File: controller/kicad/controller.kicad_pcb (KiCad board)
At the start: 2 copper layers, 90 x 80 mm, 27 parts, among them J1 pcie_98, U1 WeAct_STM32H750_Module, U10 ESD5344D, U11 ESD5344D, U12 ESD5344D, U13 ESD5344D, U14 ESD5344D, U15 ESD5344D, U16 ESD5344D, U17 ESD5344D, U18 ESD5344D, U19 ESD5344D, U2 ESD5344D, U20 ESD5344D, U21 ESD5344D, U3 ESD5344D, U4 ESD5344D, U5 ESD5344D, U6 ESD5344D, U7 ESD5344D, U8 ESD5344D, U9 ESD5344D

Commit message: Added Controller doc and added an optional jumper to short the Schottky diode.
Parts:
- added R1: 0R, Resistor_SMD:R_0805_2012Metric, F.Cu at (56.3, 38.7)
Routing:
- net /+5VBUS: track 36.5 -> 39.0 mm
- net /+5V: track 139.9 -> 142.4 mm
- net /PB13: track 88.2 -> 87.3 mm
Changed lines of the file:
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@@
     (property "ki_keywords" "diode Schottky")
     (attr smd)
-    (fp_text reference "D1" (at 0 -2.1942 -180) (layer "F.SilkS")
+    (fp_text reference "D1" (at -0.0762 2.073 -180) (layer "F.SilkS")
         (effects (font (size 1 1) (thickness 0.15)))
     )
@@
     (property "ki_keywords" "cap capacitor")
     (attr smd)
-    (fp_text reference "C2" (at 0 -3.7) (layer "F.SilkS")
+    (fp_text reference "C2" (at -0.086 3.8354) (layer "F.SilkS")
         (effects (font (size 1 1) (thickness 0.15)))
     )
@@
       (scale (xyz 1 1 1))
       (rotate (xyz 0 0 90))
+    )
+  )
+  (footprint "Resistor_SMD:R_0805_2012Metric" (layer "F.Cu")
+    (at 56.261 38.6842 90)
+    (descr "Resistor SMD 0805 (2012 Metric), square (rectangular) end terminal, IPC_7351 nominal, (Body size source: IPC-SM-782 page 72, https://www.pcb-3d.com/wordpress/wp-content/uploads/ipc-sm-782a_amendment_1_and_2.pdf), generated with kicad-footprint-generator")
+    (tags "resistor")
+    (property "LCSC" "C17477")
+    (property "Sheetfile" "controller.kicad_sch")
+    (property "Sheetname" "")
+    (property "dnp" "")
+    (property "exclude_from_bom" "")
+    (property "ki_description" "Resistor, US symbol")
+    (property "ki_keywords" "R res resistor")
+    (attr smd exclude_from_bom)
+    (fp_text reference "R1" (at -0.1524 1.8796 180) (layer "F.SilkS")
+        (effects (font (size 1 1) (thickness 0.15)))
+    )
+    (fp_text value "0R" (at 0 1.65 90) (layer "F.Fab")
+        (effects (font (size 1 1) (thickness 0.15)))
+    )
+    (fp_text user "${REFERENCE}" (at 0 0 90) (layer "F.Fab")
+        (effects (font (size 0.5 0.5) (thickness 0.08)))
+    )
+    (fp_line (start -0.227064 -0.735) (end 0.227064 -0.735)
+      (stroke (width 0.12) (type solid)) (layer "F.SilkS"))
+    (fp_line (start -0.227064 0.735) (end 0.227064 0.735)
+      (stroke (width 0.12) (type solid)) (layer "F.SilkS"))
+    (fp_line (start -1.68 -0.95) (end 1.68 -0.95)
+      (stroke (width 0.05) (type solid)) (layer "F.CrtYd"))
+    (fp_line (start -1.68 0.95) (end -1.68 -0.95)
+      (stroke (width 0.05) (type solid)) (layer "F.CrtYd"))
+    (fp_line (start 1.68 -0.95) (end 1.68 0.95)
+      (stroke (width 0.05) (type solid)) (layer "F.CrtYd"))
+    (fp_line (start 1.68 0.95) (end -1.68 0.95)
+      (stroke (width 0.05) (type solid)) (layer "F.CrtYd"))
+    (fp_line (start -1 -0.625) (end 1 -0.625)
+      (stroke (width 0.1) (type solid)) (layer "F.Fab"))
+    (fp_line (start -1 0.625) (end -1 -0.625)
+      (stroke (width 0.1) (type solid)) (layer "F.Fab"))
+    (fp_line (start 1 -0.625) (end 1 0.625)
+      (stroke (width 0.1) (type solid)) (layer "F.Fab"))
+    (fp_line (start 1 0.625) (end -1 0.625)
+      (stroke (width 0.1) (type solid)) (layer "F.Fab"))
+    (pad "1" smd roundrect (at -0.9125 0 90) (size 1.025 1.4) (layers "F.Cu" "F.Paste" "F.Mask") (roundrect_rratio 0.243902)
+      (net 3 "/+5VBUS") (pintype "passive"))
+    (pad "2" smd roundrect (at 0.9125 0 90) (size 1.025 1.4) (layers "F.Cu" "F.Paste" "F.Mask") (roundrect_rratio 0.243902)
+      (net 98 "/+5V") (pintype "passive"))
+    (model "${KICAD6_3DMODEL_DIR}/Resistor_SMD.3dshapes/R_0805_2012Metric.wrl"
+      (offset (xyz 0 0 0))
+      (scale (xyz 1 1 1))
+      (rotate (xyz 0 0 0))
     )
   )
@@
   (segment (start 58.5 53.4962) (end 58.4962 53.4924) (width 0.6096) (layer "F.Cu") (net 3))
   (segment (start 58.4962 53.4924) (end 58.5216 53.467) (width 0.6096) (layer "F.Cu") (net 3))
+  (segment (start 55.4981 40.3596) (end 56.261 39.5967) (width 0.762) (layer "F.Cu") (net 3))
   (segment (start 58.9534 44.196) (end 54.2798 44.196) (width 1.524) (layer "F.Cu") (net 3))
   (segment (start 58.5216 53.467) (end 61.4934 53.467) (width 0.6096) (layer "F.Cu") (net 3))
+  (segment (start 54.0668 40.3596) (end 55.4981 40.3596) (width 0.762) (layer "F.Cu") (net 3))
   (segment (start 60.5 53.4698) (end 60.5028 53.467) (width 0.6096) (layer "F.Cu") (net 3))
   (segment (start 61.5625 44) (end 62.4375 44) (width 0.2286) (layer "F.Cu") (net 3))
   (segment (start 58.9534 44.196) (end 58.9534 53.1876) (width 1.524) (layer "F.Cu") (net 3))
   (segment (start 62.5 56.55) (end 62.5 53.4703) (width 0.1524) (layer "F.Cu") (net 4))
-  (segment (start 63.0036 43.7504) (end 57.2262 37.973) (width 0.1524) (layer "F.Cu") (net 4))
-  (segment (start 62.4375 44.5) (end 62.8572 44.5) (width 0.1524) (layer "F.Cu") (net 4))
   (segment (start 61.5625 44.5) (end 62.1327 44.5) (width 0.1524) (layer "F.Cu") (net 4))
   (segment (start 62.5 53.4703) (end 59.974098 50.944398) (width 0.1524) (layer "F.Cu") (net 4))
+  (segment (start 63.0036 44.3536) (end 63.0036 43.7504) (width 0.1524) (layer "F.Cu") (net 4))
   (segment (start 60.618958 44.4486) (end 61.5111 44.4486) (width 0.1524) (layer "F.Cu") (net 4))
   (segment (start 59.974098 45.09346) (end 60.618958 44.4486) (width 0.1524) (layer "F.Cu") (net 4))
+  (segment (start 62.8572 44.5) (end 63.0036 44.3536) (width 0.1524) (layer "F.Cu") (net 4))
   (segment (start 59.974098 50.944398) (end 59.974098 45.09346) (width 0.1524) (layer "F.Cu") (net 4))
-  (segment (start 57.2262 -10.8862) (end 67.8 -21.46) (width 0.1524) (layer "F.Cu") (net 4))
-  (segment (start 57.2262 37.973) (end 57.2262 -10.8862) (width 0.1524) (layer "F.Cu") (net 4))
-  (segment (start 62.8572 44.5) (end 63.0036 44.3536) (width 0.1524) (layer "F.Cu") (net 4))
+  (segment (start 58.2676 -11.9276) (end 67.8 -21.46) (width 0.1524) (layer "F.Cu") (net 4))
+  (segment (start 58.2676 39.0144) (end 58.2676 -11.9276) (width 0.1524) (layer "F.Cu") (net 4))
+  (segment (start 62.4375 44.5) (end 62.8572 44.5) (width 0.1524) (layer "F.Cu") (net 4))
   (segment (start 61.5111 44.4486) (end 61.5625 44.5) (width 0.1524) (layer "F.Cu") (net 4))
-  (segment (start 63.0036 44.3536) (end 63.0036 43.7504) (width 0.1524) (layer "F.Cu") (net 4))
+  (segment (start 63.0036 43.7504) (end 58.2676 39.0144) (width 0.1524) (layer "F.Cu") (net 4))
   (segment (start 85.387798 52.774198) (end 85.5 52.8864) (width 0.1524) (layer "F.Cu") (net 5))
   (segment (start 88.4428 44.990106) (end 88.4428 -3.3572) (width 0.1524) (layer "F.Cu") (net 5))
@@
   (segment (start 106.5625 49.5) (end 107.4375 49.5) (width 0.1524) (layer "F.Cu") (net 94))
   (segment (start 108.458 -19.9644) (end 108.458 -22.733) (width 1.524) (layer "F.Cu") (net 98))
+  (segment (start 54.0668 37.0596) (end 55.5489 37.0596) (width 0.762) (layer "F.Cu") (net 98))
   (segment (start 105.9 -18.92) (end 107.4136 -18.92) (width 1.524) (layer "F.Cu") (net 98))
   (segment (start 109.027 -18.8214) (end 108.8644 -18.8214) (width 0.3048) (layer "F.Cu") (net 98))
@@
   (segment (start 66.1416 -24.1046) (end 54.0668 -12.0298) (width 1.524) (layer "F.Cu") (net 98))
   (segment (start 107.0864 -24.1046) (end 66.1416 -24.1046) (width 1.524) (layer "F.Cu") (net 98))
+  (segment (start 55.5489 37.0596) (end 56.261 37.7717) (width 0.762) (layer "F.Cu") (net 98))
   (segment (start 108.2802 -19.7866) (end 108.458 -19.9644) (width 1.524) (layer "F.Cu") (net 98))
   (segment (start 108.8644 -18.8214) (end 108.2802 -19.4056) (width 0.3048) (layer "F.Cu") (net 98))

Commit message: Fixed the orientation of the 100uf capacitors for JLCPCB.
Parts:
- C1, C2: footprint Capacitor_SMD:CP_Elec_5x5.4 -> controller:CP_Elec_5x5.4_JLCPCB
- turned C1 to 0 degrees
- turned C2 to 0 degrees
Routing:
- net /+5V: track 142.4 -> 143.4 mm

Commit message: Spaced the PCB traks.
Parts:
- moved U1 0.13 mm to (86.9, 5.33)
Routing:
- net /PB11: track 98.1 -> 84.0 mm
- net /PE15: track 91.4 -> 80.0 mm
- net /PE13: track 85.9 -> 76.8 mm
- net /PE11: track 81.8 -> 74.7 mm
- net /PA6: track 64.6 -> 60.4 mm
- net /PB0: track 70.0 -> 65.9 mm
- net /PE9: track 76.1 -> 72.5 mm
- net /PC4: track 65.9 -> 62.7 mm
- net /PB2: track 71.9 -> 69.0 mm
- net /PC13: track 43.5 -> 41.3 mm
- net /PE7: track 71.7 -> 69.6 mm
- net /PC0: track 46.2 -> 44.4 mm
- net /PB1: track 68.0 -> 66.3 mm
- net /PA5: track 59.5 -> 57.9 mm
- net /PE8: track 73.3 -> 71.8 mm
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
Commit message: Simplified the controller board: removed the jumper resistor.
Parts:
- removed R1: 0R, Resistor_SMD:R_0805_2012Metric
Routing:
- net /+5VBUS: track 39.0 -> 36.5 mm
- net /+5V: track 143.2 -> 140.7 mm
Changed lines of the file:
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@@
     (property "ki_keywords" "diode Schottky")
     (attr smd)
-    (fp_text reference "D1" (at -0.0762 2.073 -180) (layer "F.SilkS")
+    (fp_text reference "D1" (at -0.254 -2.245 -180) (layer "F.SilkS")
         (effects (font (size 1 1) (thickness 0.15)))
     )
@@
     (property "ki_keywords" "cap capacitor")
     (attr smd)
-    (fp_text reference "C2" (at 0 3.7) (layer "F.SilkS")
+    (fp_text reference "C2" (at -0.0156 4.0132) (layer "F.SilkS")
         (effects (font (size 1 1) (thickness 0.15)))
     )
@@
       (scale (xyz 1 1 1))
       (rotate (xyz 0 0 90))
-    )
-  )
-  (footprint "Resistor_SMD:R_0805_2012Metric" (layer "F.Cu")
-    (at 56.261 38.6842 90)
-    (descr "Resistor SMD 0805 (2012 Metric), square (rectangular) end terminal, IPC_7351 nominal, (Body size source: IPC-SM-782 page 72, https://www.pcb-3d.com/wordpress/wp-content/uploads/ipc-sm-782a_amendment_1_and_2.pdf), generated with kicad-footprint-generator")
-    (tags "resistor")
-    (property "LCSC" "C17477")
-    (property "Sheetfile" "controller.kicad_sch")
-    (property "Sheetname" "")
-    (property "dnp" "")
-    (property "exclude_from_bom" "")
-    (property "ki_description" "Resistor, US symbol")
-    (property "ki_keywords" "R res resistor")
-    (attr smd exclude_from_bom)
-    (fp_text reference "R1" (at -0.1524 1.8796 180) (layer "F.SilkS")
-        (effects (font (size 1 1) (thickness 0.15)))
-    )
-    (fp_text value "0R" (at 0 1.65 90) (layer "F.Fab")
-        (effects (font (size 1 1) (thickness 0.15)))
-    )
-    (fp_text user "${REFERENCE}" (at 0 0 90) (layer "F.Fab")
-        (effects (font (size 0.5 0.5) (thickness 0.08)))
-    )
-    (fp_line (start -0.227064 -0.735) (end 0.227064 -0.735)
-      (stroke (width 0.12) (type solid)) (layer "F.SilkS"))
-    (fp_line (start -0.227064 0.735) (end 0.227064 0.735)
-      (stroke (width 0.12) (type solid)) (layer "F.SilkS"))
-    (fp_line (start -1.68 -0.95) (end 1.68 -0.95)
-      (stroke (width 0.05) (type solid)) (layer "F.CrtYd"))
-    (fp_line (start -1.68 0.95) (end -1.68 -0.95)
-      (stroke (width 0.05) (type solid)) (layer "F.CrtYd"))
-    (fp_line (start 1.68 -0.95) (end 1.68 0.95)
-      (stroke (width 0.05) (type solid)) (layer "F.CrtYd"))
-    (fp_line (start 1.68 0.95) (end -1.68 0.95)
-      (stroke (width 0.05) (type solid)) (layer "F.CrtYd"))
-    (fp_line (start -1 -0.625) (end 1 -0.625)
-      (stroke (width 0.1) (type solid)) (layer "F.Fab"))
-    (fp_line (start -1 0.625) (end -1 -0.625)
-      (stroke (width 0.1) (type solid)) (layer "F.Fab"))
-    (fp_line (start 1 -0.625) (end 1 0.625)
-      (stroke (width 0.1) (type solid)) (layer "F.Fab"))
-    (fp_line (start 1 0.625) (end -1 0.625)
-      (stroke (width 0.1) (type solid)) (layer "F.Fab"))
-    (pad "1" smd roundrect (at -0.9125 0 90) (size 1.025 1.4) (layers "F.Cu" "F.Paste" "F.Mask") (roundrect_rratio 0.243902439)
-      (net 3 "/+5VBUS") (pintype "passive"))
-    (pad "2" smd roundrect (at 0.9125 0 90) (size 1.025 1.4) (layers "F.Cu" "F.Paste" "F.Mask") (roundrect_rratio 0.243902439)
-      (net 98 "/+5V") (pintype "passive"))
-    (model "${KICAD6_3DMODEL_DIR}/Resistor_SMD.3dshapes/R_0805_2012Metric.wrl"
-      (offset (xyz 0 0 0))
-      (scale (xyz 1 1 1))
-      (rotate (xyz 0 0 0))
     )
   )
@@
   (segment (start 58.5 53.4962) (end 58.4962 53.4924) (width 0.6096) (layer "F.Cu") (net 3))
   (segment (start 58.4962 53.4924) (end 58.5216 53.467) (width 0.6096) (layer "F.Cu") (net 3))
-  (segment (start 55.4981 40.3596) (end 56.261 39.5967) (width 0.762) (layer "F.Cu") (net 3))
   (segment (start 58.9534 44.196) (end 54.2798 44.196) (width 1.524) (layer "F.Cu") (net 3))
   (segment (start 58.5216 53.467) (end 61.4934 53.467) (width 0.6096) (layer "F.Cu") (net 3))
-  (segment (start 54.0668 40.3596) (end 55.4981 40.3596) (width 0.762) (layer "F.Cu") (net 3))
   (segment (start 60.5 53.4698) (end 60.5028 53.467) (width 0.6096) (layer "F.Cu") (net 3))
   (segment (start 61.5625 44) (end 62.4375 44) (width 0.2286) (layer "F.Cu") (net 3))
@@
   (segment (start 70.3732 31.9888) (end 70.358 32.004) (width 0.3048) (layer "F.Cu") (net 98))
   (segment (start 108.458 -19.9644) (end 108.458 -22.733) (width 1.524) (layer "F.Cu") (net 98))
-  (segment (start 54.0668 37.0596) (end 55.5489 37.0596) (width 0.762) (layer "F.Cu") (net 98))
   (segment (start 107.4136 -18.92) (end 108.2802 -19.7866) (width 1.524) (layer "F.Cu") (net 98))
   (segment (start 108.458 -22.733) (end 107.0864 -24.1046) (width 1.524) (layer "F.Cu") (net 98))
@@
   (segment (start 107.5122 -18.8214) (end 107.4136 -18.92) (width 0.3048) (layer "F.Cu") (net 98))
   (segment (start 107.0864 -24.1046) (end 66.1416 -24.1046) (width 1.524) (layer "F.Cu") (net 98))
-  (segment (start 55.5489 37.0596) (end 56.261 37.7717) (width 0.762) (layer "F.Cu") (net 98))
   (segment (start 108.2802 -19.7866) (end 108.458 -19.9644) (width 1.524) (layer "F.Cu") (net 98))
   (segment (start 54.0668 -12.0298) (end 54.0668 37.0596) (width 1.524) (layer "F.Cu") (net 98))

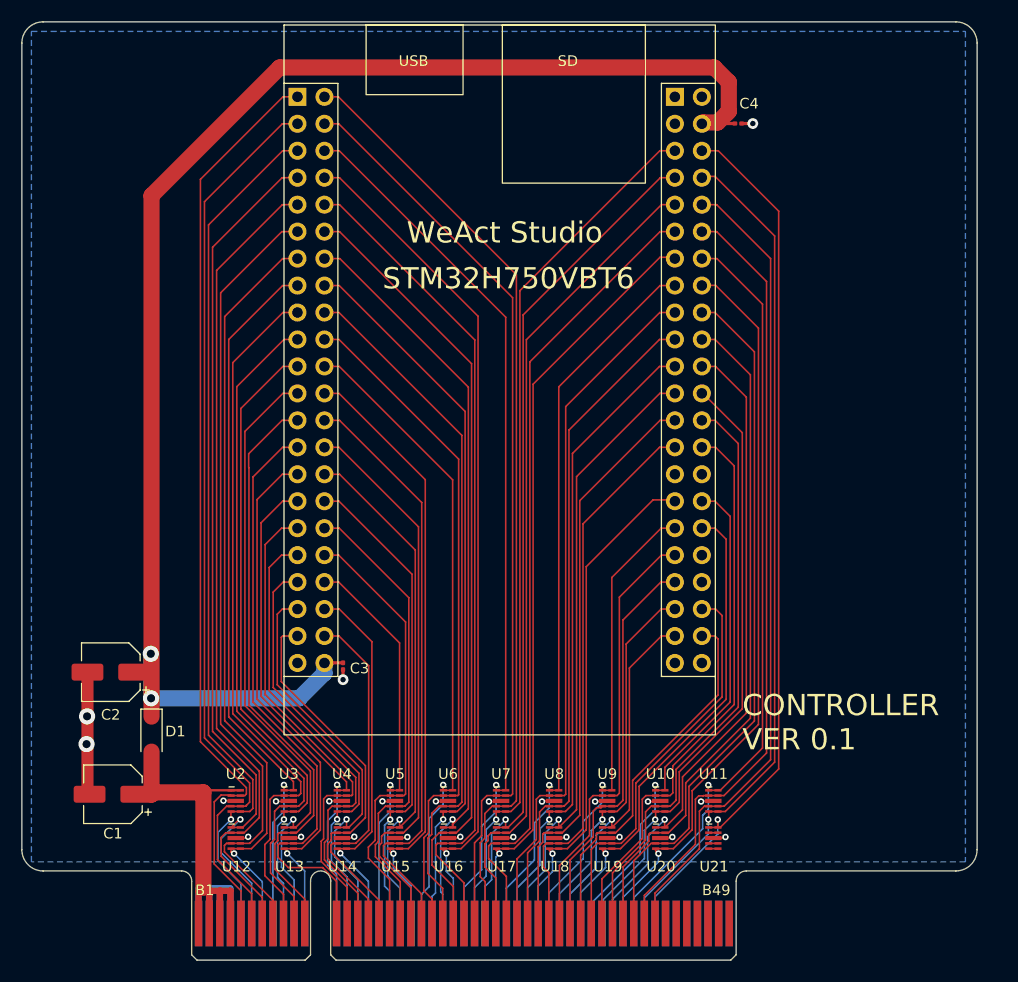
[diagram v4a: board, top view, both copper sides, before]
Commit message: Refactored libraries to have common symbols, footprints, and 3D models in the common kicad project.
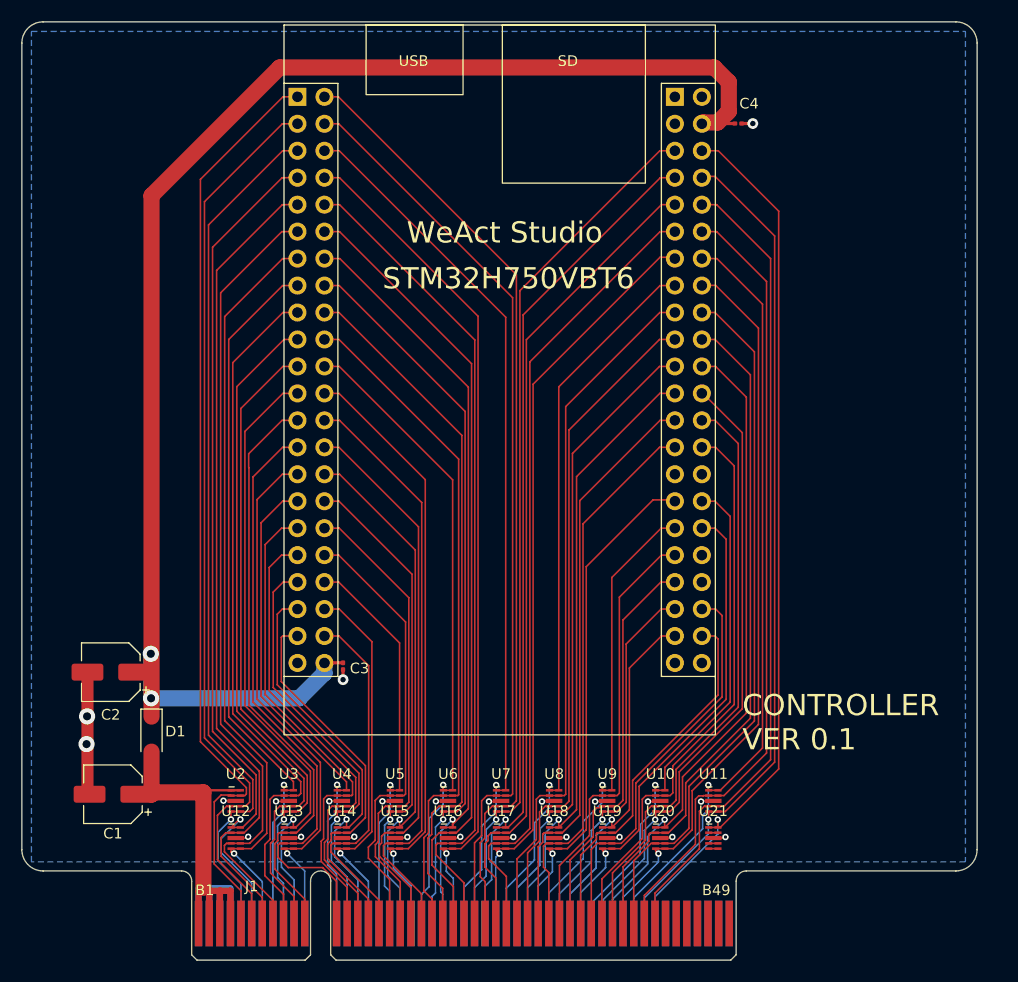
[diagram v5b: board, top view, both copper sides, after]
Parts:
- J1: footprint controller:pcie_98_edge -> common:PCIE_98_CARD
- U10, U11, U12, U13, U14, U15, U16, U17, U18, U19, U2, U20, U21, U3, U4, U5, U6, U7, U8, U9: footprint controller:Diodes_UDFN-10_1.0x2.5mm_P0.5mm -> common:Diodes_UDFN-10_1.0x2.5mm_P0.5mm
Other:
- board size 90 x 80 mm -> 90 x 88.4 mm
